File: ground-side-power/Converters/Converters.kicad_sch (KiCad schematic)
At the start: 29 parts, among them J10 Conn_01x02_Female, J11 Conn_01x03_Female, J12 Conn_01x03_Female, J13 DAQ Voltage Sensing, J14 DAQ Current Sensing, U3 K7805-3AR3, U4 INA180, U5 INA180, U6 URB2424LD-20WR3

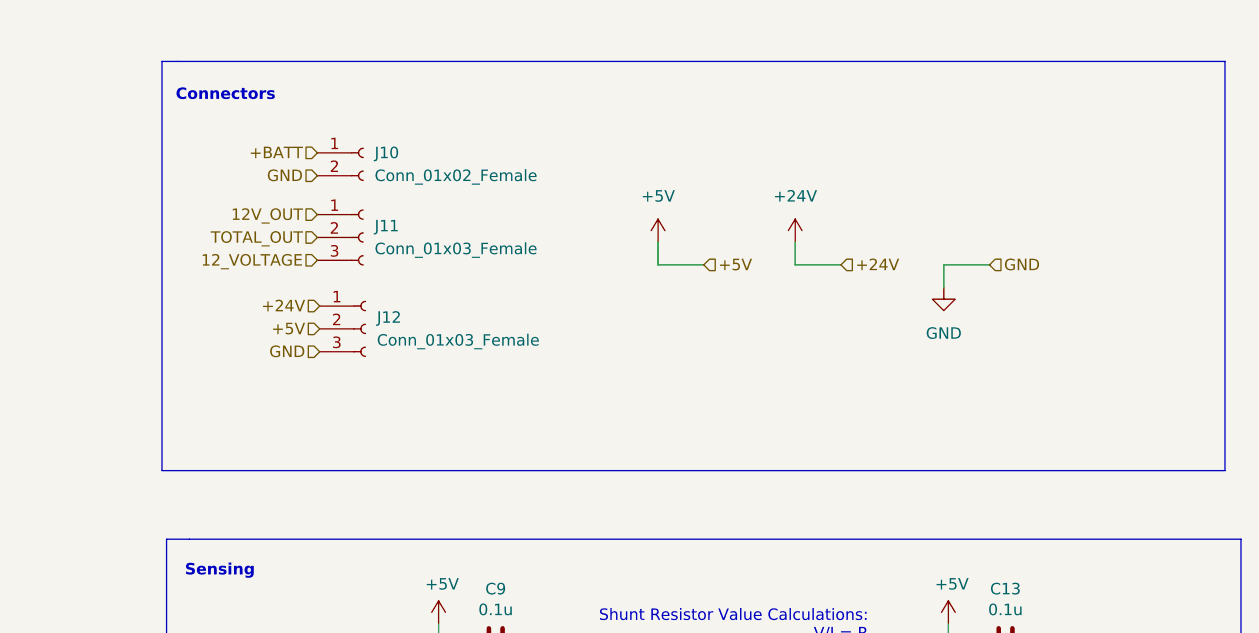
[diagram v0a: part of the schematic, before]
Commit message: Created layout for the footprints for each board
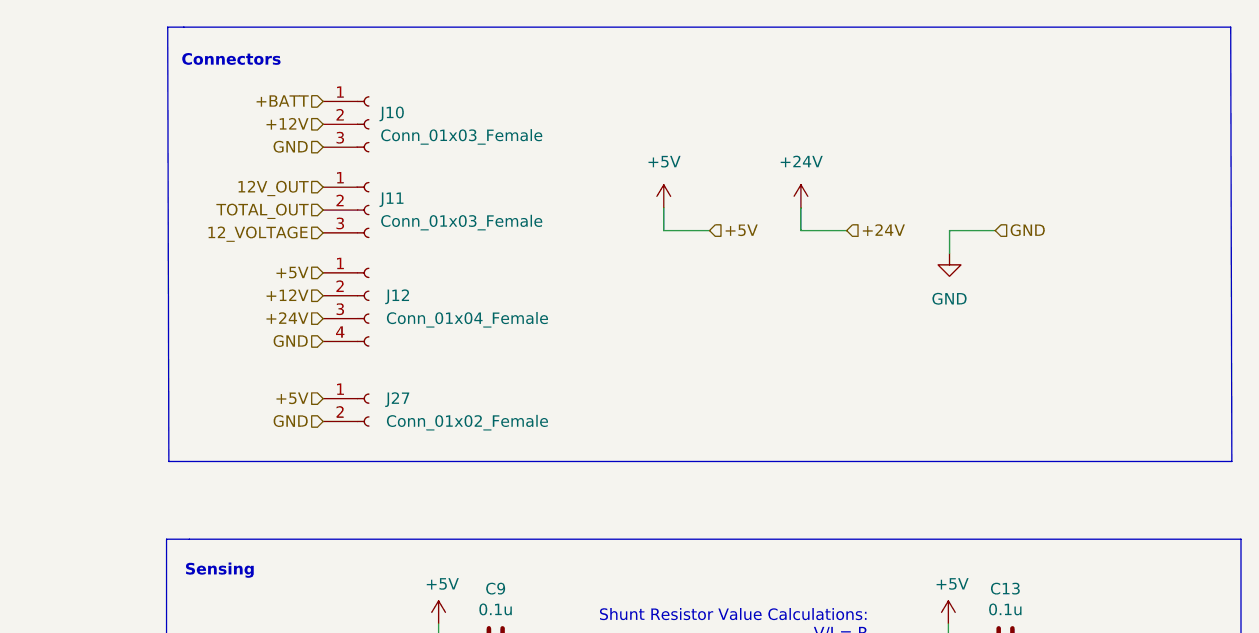
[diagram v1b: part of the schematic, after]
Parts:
- removed J10: Conn_01x02_Female, GSP:OSTTA020161, symbol Connector:Conn_01x02_Female
- removed J12: Conn_01x03_Female, GSP:TB005-762-03BE, symbol Connector:Conn_01x03_Female
- added J10: Conn_01x03_Female, GSP:TB005-762-03BE, symbol Connector:Conn_01x03_Female
- added J12: Conn_01x04_Female, GSP:EB21A-04-D, symbol Connector:Conn_01x04_Female
- added J27: Conn_01x02_Female, GSP:OSTTA020161, symbol Connector:Conn_01x02_Female
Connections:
- net +24V: now also J12.3 (Pin_3)
- net +5V: now also J12.1 (Pin_1), J27.1 (Pin_1)
- net +BATT: now also J10.1 (Pin_1)
- net GND: now also J10.3 (Pin_3), J12.4 (Pin_4), J27.2 (Pin_2)
- new net +12V: J10.2 (Pin_2), J12.2 (Pin_2)
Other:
- moved on the sheet: J11

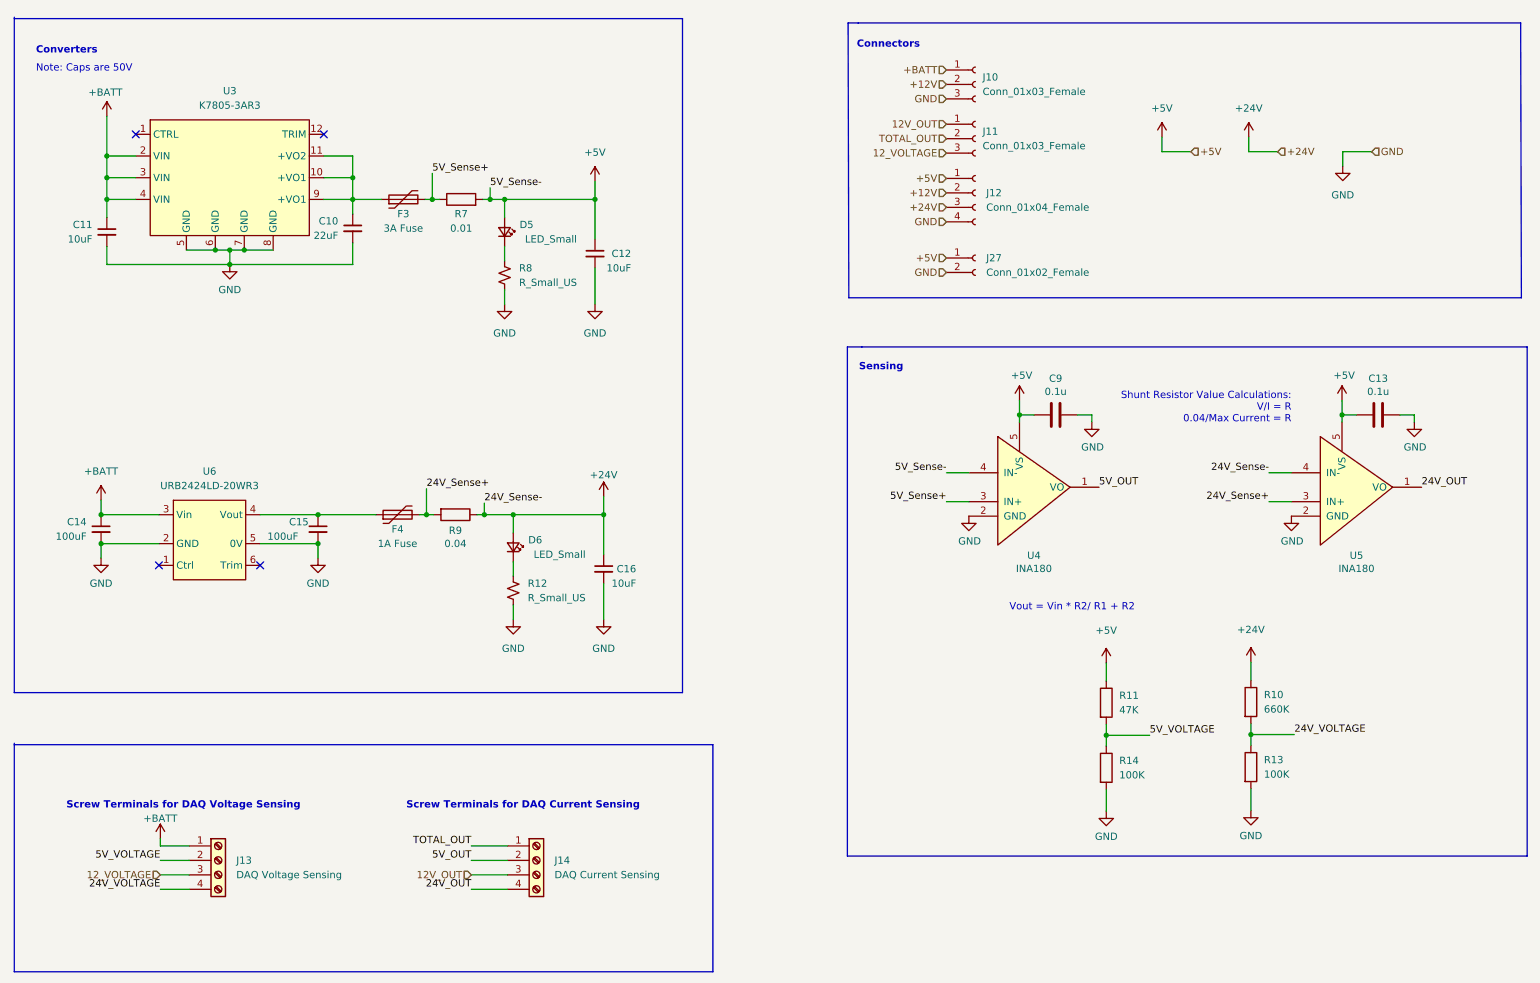
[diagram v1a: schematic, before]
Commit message: Added Fan Headers + Thermistor
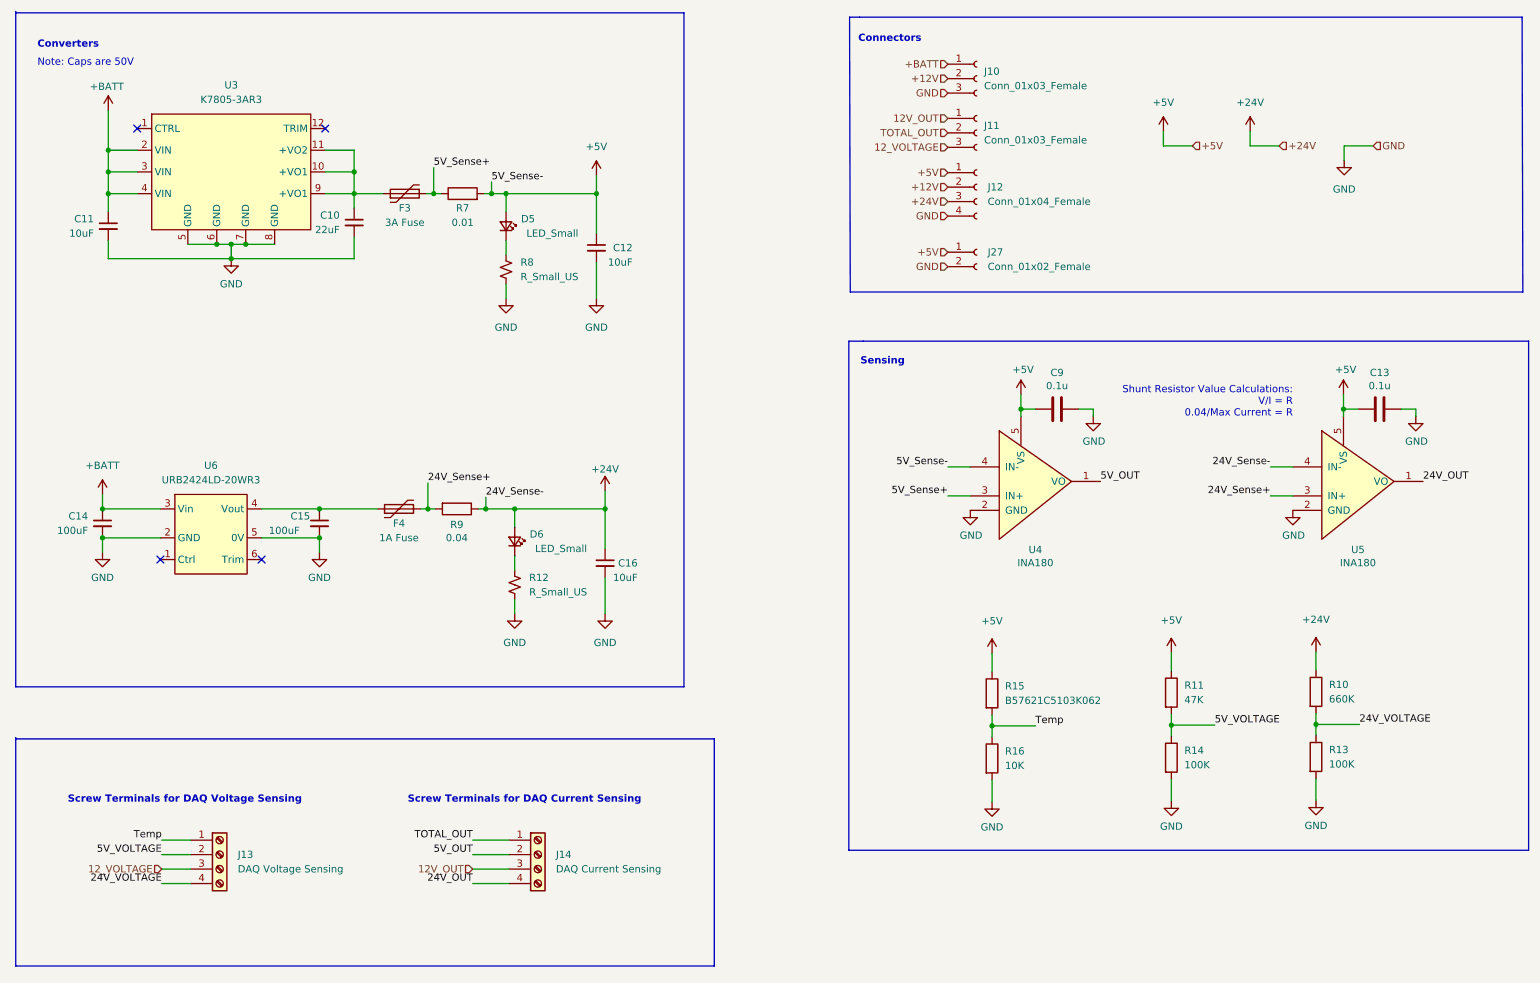
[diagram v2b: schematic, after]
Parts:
- added R15: B57621C5103K062, Resistor_SMD:R_1206_3216Metric_Pad1.30x1.75mm_HandSolder, symbol Device:R
- added R16: 10K, Resistor_SMD:R_0402_1005Metric_Pad0.72x0.64mm_HandSolder, symbol Device:R
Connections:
- net +5V: now also R15.1
- net +BATT: no longer J13.1 (Pin_1)
- net GND: now also R16.2
- new net Temp: J13.1 (Pin_1), R15.2, R16.1
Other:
- note removed: "Vout = Vin * R2/ R1 + R2"

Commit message: PCB Layout First Draft
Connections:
- net +12V: now also J12.3 (Pin_3); no longer J12.2 (Pin_2)
- net +24V: now also J12.1 (Pin_1); no longer J12.3 (Pin_3)
- net +5V: now also J12.4 (Pin_4); no longer J12.1 (Pin_1)
- net 12V_OUT: now also J11.3 (Pin_3); no longer J11.1 (Pin_1)
- net 12_VOLTAGE: now also J11.1 (Pin_1); no longer J11.3 (Pin_3)
- net GND: now also J12.2 (Pin_2); no longer J12.4 (Pin_4)
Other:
- moved on the sheet: J12

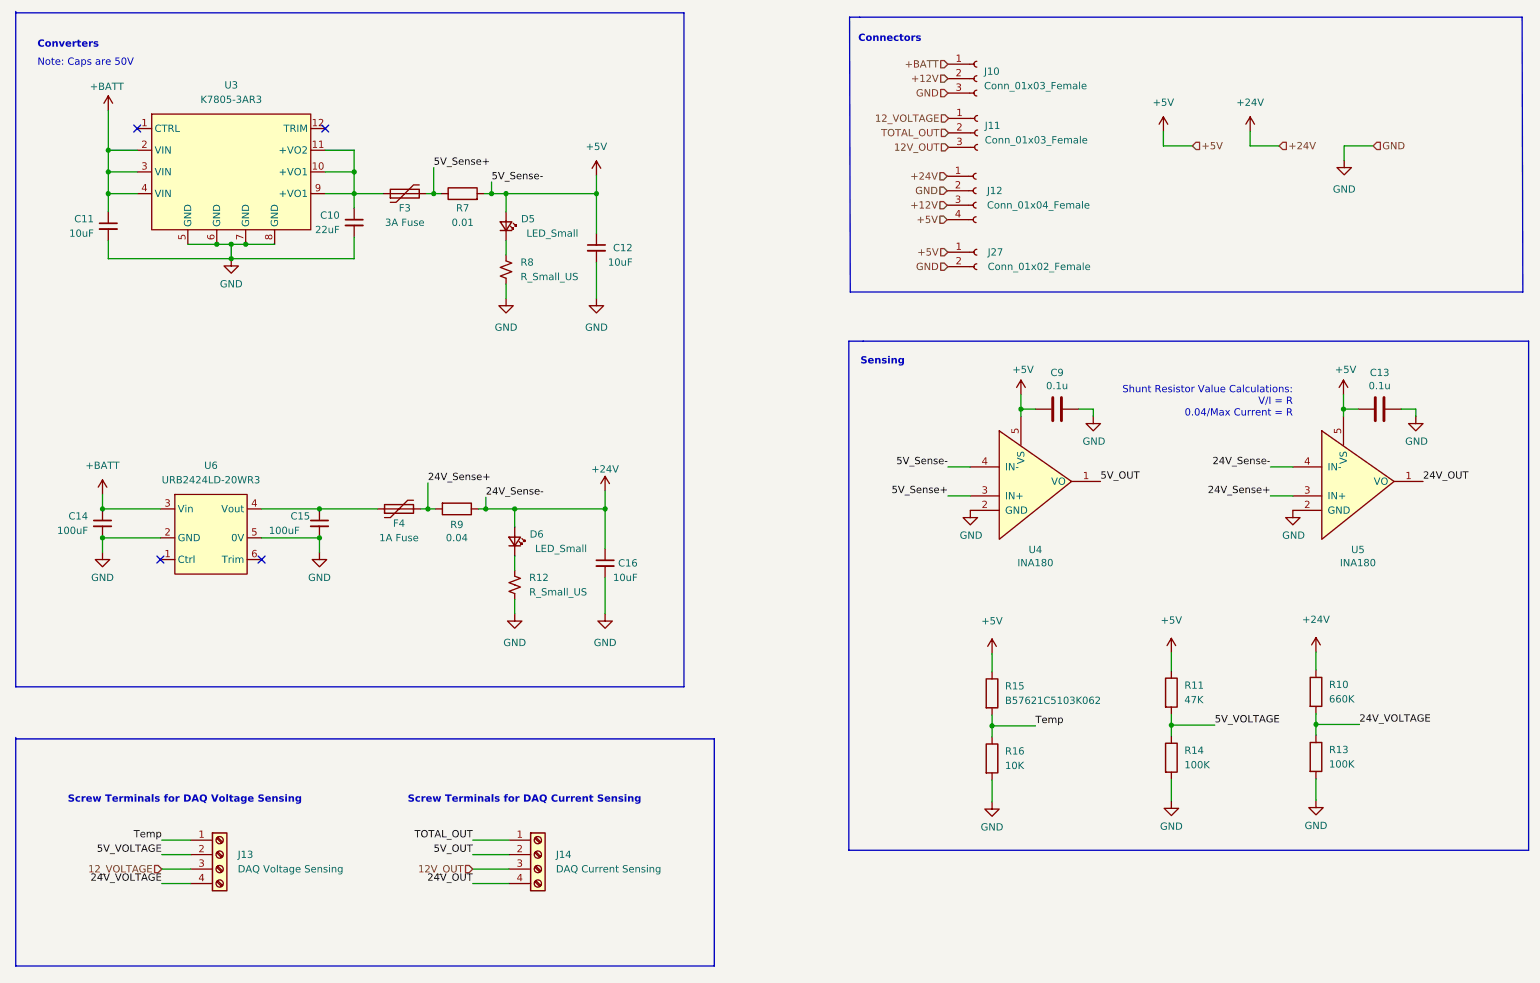
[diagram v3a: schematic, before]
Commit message: Address Input and Converter Comments
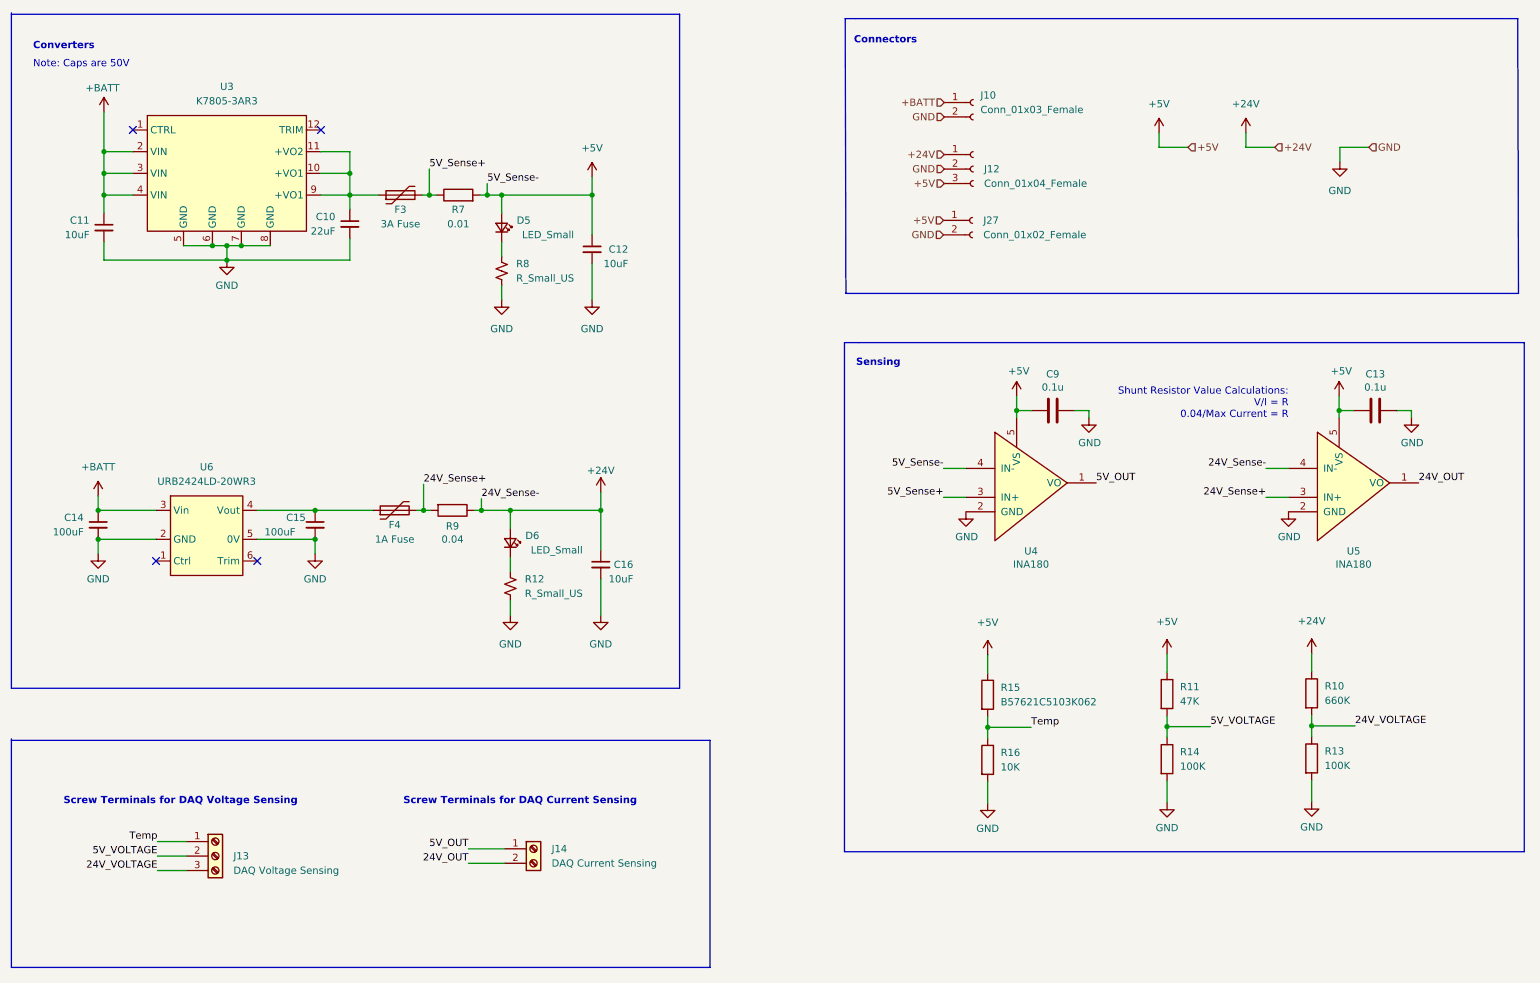
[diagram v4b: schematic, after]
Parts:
- removed J10, J11: Conn_01x03_Female, GSP:TB005-762-03BE, symbol Connector:Conn_01x03_Female
- removed J12: Conn_01x04_Female, GSP:EB21A-04-D, symbol Connector:Conn_01x04_Female
- removed J13: DAQ Voltage Sensing, GSP:EB21A-04-D, symbol Connector:Screw_Terminal_01x04
- removed J14: DAQ Current Sensing, GSP:EB21A-04-D, symbol Connector:Screw_Terminal_01x04
- added J10: Conn_01x03_Female, GSP:1935310, symbol Connector:Conn_01x02_Female
- added J12: Conn_01x04_Female, GSP:1935323, symbol Connector:Conn_01x03_Female
- added J13: DAQ Voltage Sensing, GSP:1935323, symbol Connector:Screw_Terminal_01x03
- added J14: DAQ Current Sensing, GSP:1935310, symbol Connector:Screw_Terminal_01x02
- C14, C15: footprint Capacitor_SMD:C_1206_3216Metric_Pad1.33x1.80mm_HandSolder -> Capacitor_THT:CP_Radial_D6.3mm_P2.50mm
- D5, D6: footprint Diode_SMD:D_0805_2012Metric -> Diode_SMD:D_1206_3216Metric_Pad1.42x1.75mm_HandSolder
- F3, F4: footprint Fuse:Fuse_1206_3216Metric_Pad1.42x1.75mm_HandSolder -> Fuse:Fuseholder_Clip-6.3x32mm_Littelfuse_102_122_Inline_P34.21x7.62mm_D1.98mm_Horizontal
- J27: footprint GSP:OSTTA020161 -> GSP:1935310
- R10, R11: footprint Resistor_SMD:R_0603_1608Metric_Pad0.98x0.95mm_HandSolder -> Resistor_SMD:R_0805_2012Metric_Pad1.20x1.40mm_HandSolder
- R12, R8: footprint Resistor_SMD:R_1206_3216Metric_Pad1.30x1.75mm_HandSolder -> Resistor_SMD:R_0805_2012Metric_Pad1.20x1.40mm_HandSolder
- R13, R14, R16: footprint Resistor_SMD:R_0402_1005Metric_Pad0.72x0.64mm_HandSolder -> Resistor_SMD:R_0805_2012Metric_Pad1.20x1.40mm_HandSolder
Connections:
- net +24V: now also J12.1 (Pin_1)
- net +5V: now also J12.3 (Pin_3)
- net +BATT: now also J10.1 (Pin_1)
- net 24V_OUT: now also J14.2 (Pin_2)
- net 24V_VOLTAGE: now also J13.3 (Pin_3)
- net 5V_OUT: now also J14.1 (Pin_1)
- net 5V_VOLTAGE: now also J13.2 (Pin_2)
- net GND: now also J10.2 (Pin_2), J12.2 (Pin_2)
- net Temp: now also J13.1 (Pin_1)
